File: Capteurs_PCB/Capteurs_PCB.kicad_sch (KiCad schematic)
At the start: 24 parts, among them J1 Conn_01x04, J101 Conn_01x03, J103 Conn_02x20_Odd_Even, J104 Conn_ST_STDC14, J2 Conn_01x03, J3 Alim_Prop2, J4 Conn_01x02, J5 Alim_Prop1, J6 Conn_01x03, J7 Conn_01x03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

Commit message: Problème réglé
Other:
- sheet Regulation ports: added 12V; removed 7.4V
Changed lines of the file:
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@@
-    )
-  )
-  (symbol (lib_id "power:+7.5V") (at 143.51 114.3 270) (unit 1)
-    (in_bom yes) (on_board yes) (dnp no) (fields_autoplaced)
-    (property "Reference" "#PWR0119" (at 139.7 114.3 0)
-      (effects (font (size 1.27 1.27)) hide)
-    )
-    (property "Value" "+7.4V" (at 147.32 114.935 90)
-      (effects (font (size 1.27 1.27)) (justify left))
-    )
-    (property "Footprint" "" (at 143.51 114.3 0)
-      (effects (font (size 1.27 1.27)) hide)
-    )
-    (property "Datasheet" "" (at 143.51 114.3 0)
-      (effects (font (size 1.27 1.27)) hide)
-    )
-    (pin "1")
-    (instances
-      (project "Capteurs_PCB"
-        (path "/1101af8f-9425-4102-9245-339dc54562bf"
-          (reference "#PWR0119") (unit 1)
-        )
-      )
     )
   )
@@
       (effects (font (size 1.27 1.27)) (justify right))
     )
-    (pin "7.4V" input (at 142.24 114.3 0)
+    (pin "12V" input (at 142.24 114.3 0)
       (effects (font (size 1.27 1.27)) (justify right))
     )

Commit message: modifs kicad
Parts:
- removed J3: Alim_Prop2, Connector_Hirose:Hirose_DF13-02P-1.25DSA_1x02_P1.25mm_Vertical, symbol Connector:Conn_01x02_Socket
- removed J5: Alim_Prop1, Connector_Hirose:Hirose_DF13-02P-1.25DSA_1x02_P1.25mm_Vertical, symbol Connector:Conn_01x02_Socket
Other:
- sheet Regulation ports: added 7.5V; removed 12V
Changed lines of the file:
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@@
+    (stroke (width 0) (type default))
+  )
+  (wire (pts (xy 62.23 76.2) (xy 68.58 76.2))
     (stroke (width 0) (type default))
   )
@@
     (stroke (width 0) (type default))
   )
-  (wire (pts (xy 212.09 45.72) (xy 224.79 45.72))
-    (stroke (width 0) (type default))
-  )
   (wire (pts (xy 105.41 114.3) (xy 114.3 114.3))
     (stroke (width 0) (type default))
@@
     (stroke (width 0) (type default))
   )
-  (wire (pts (xy 176.53 46.99) (xy 187.96 46.99))
-    (stroke (width 0) (type default))
-  )
   (wire (pts (xy 144.78 39.37) (xy 143.51 39.37))
     (stroke (width 0) (type default))
@@
     (stroke (width 0) (type default))
   )
-  (wire (pts (xy 176.53 49.53) (xy 176.53 50.8))
-    (stroke (width 0) (type default))
-  )
   (wire (pts (xy 224.79 77.47) (xy 226.06 77.47))
     (stroke (width 0) (type default))
@@
     (stroke (width 0) (type default))
   )
-  (wire (pts (xy 212.09 48.26) (xy 213.36 48.26))
-    (stroke (width 0) (type default))
-  )
   (wire (pts (xy 144.78 62.23) (xy 144.78 54.61))
     (stroke (width 0) (type default))
@@
   )
   (wire (pts (xy 46.99 66.04) (xy 46.99 62.23))
-    (stroke (width 0) (type default))
-  )
-  (wire (pts (xy 213.36 48.26) (xy 213.36 49.53))
     (stroke (width 0) (type default))
   )
@@
     (effects (font (size 1.27 1.27)) (justify right bottom))
   )
-  (label "V_ALIM_PROP1" (at 187.96 46.99 180) (fields_autoplaced)
-    (effects (font (size 1.27 1.27)) (justify right bottom))
-  )
   (label "Sig_LED" (at 102.87 91.44 180) (fields_autoplaced)
     (effects (font (size 1.27 1.27)) (justify right bottom))
@@
     (effects (font (size 1.27 1.27)) (justify right bottom))
   )
-  (label "V_ALIM_PROP2" (at 224.79 45.72 180) (fields_autoplaced)
+  (label "DATA1" (at 68.58 76.2 180) (fields_autoplaced)
     (effects (font (size 1.27 1.27)) (justify right bottom))
   )
@@
     (effects (font (size 1.27 1.27)) (justify left))
     (property "Intersheetrefs" "${INTERSHEET_REFS}" (at 235.9205 74.93 0)
-      (effects (font (size 1.27 1.27)) (justify left) hide)
-    )
-  )
-  (global_label "DATA1" (shape input) (at 62.23 76.2 0) (fields_autoplaced)
-    (effects (font (size 1.27 1.27)) (justify left))
-    (property "Intersheetrefs" "${INTERSHEET_REFS}" (at 70.7601 76.2 0)
       (effects (font (size 1.27 1.27)) (justify left) hide)
     )
@@
         (path "/1101af8f-9425-4102-9245-339dc54562bf"
           (reference "#PWR040") (unit 1)
-        )
-      )
-    )
-  )
-  (symbol (lib_id "Connector:Conn_01x02_Socket") (at 207.01 48.26 180) (unit 1)
-    (in_bom yes) (on_board yes) (dnp no)
-    (property "Reference" "J3" (at 207.01 39.37 0)
-      (effects (font (size 1.27 1.27)))
-    )
-    (property "Value" "Alim_Prop2" (at 207.01 41.91 0)
-      (effects (font (size 1.27 1.27)))
-    )
-    (property "Footprint" "Connector_Hirose:Hirose_DF13-02P-1.25DSA_1x02_P1.25mm_Vertical" (at 207.01 48.26 0)
-      (effects (font (size 1.27 1.27)) hide)
-    )
-    (property "Datasheet" "~" (at 207.01 48.26 0)
-      (effects (font (size 1.27 1.27)) hide)
-    )
-    (pin "1")
-    (pin "2")
-    (instances
-      (project "Capteurs_PCB"
-        (path "/1101af8f-9425-4102-9245-339dc54562bf"
-          (reference "J3") (unit 1)
         )
       )
@@
     )
   )
-  (symbol (lib_id "power:GND") (at 176.53 50.8 0) (unit 1)
-    (in_bom yes) (on_board yes) (dnp no)
-    (property "Reference" "#PWR010" (at 176.53 57.15 0)
-      (effects (font (size 1.27 1.27)) hide)
-    )
-    (property "Value" "GND" (at 176.53 55.88 0)
-      (effects (font (size 1.27 1.27)))
-    )
-    (property "Footprint" "" (at 176.53 50.8 0)
-      (effects (font (size 1.27 1.27)) hide)
-    )
-    (property "Datasheet" "" (at 176.53 50.8 0)
-      (effects (font (size 1.27 1.27)) hide)
-    )
-    (pin "1")
-    (instances
-      (project "Capteurs_PCB"
-        (path "/1101af8f-9425-4102-9245-339dc54562bf"
-          (reference "#PWR010") (unit 1)
-        )
-      )
-    )
-  )
   (symbol (lib_id "Connector_Generic:Conn_01x02") (at 238.76 30.48 180) (unit 1)
     (in_bom yes) (on_board yes) (dnp no) (fields_autoplaced)
@@
     )
   )
-  (symbol (lib_id "power:GND") (at 213.36 49.53 0) (unit 1)
-    (in_bom yes) (on_board yes) (dnp no)
-    (property "Reference" "#PWR011" (at 213.36 55.88 0)
-      (effects (font (size 1.27 1.27)) hide)
-    )
-    (property "Value" "GND" (at 213.36 54.61 0)
-      (effects (font (size 1.27 1.27)))
-    )
-    (property "Footprint" "" (at 213.36 49.53 0)
-      (effects (font (size 1.27 1.27)) hide)
-    )
-    (property "Datasheet" "" (at 213.36 49.53 0)
-      (effects (font (size 1.27 1.27)) hide)
-    )
-    (pin "1")
-    (instances
-      (project "Capteurs_PCB"
-        (path "/1101af8f-9425-4102-9245-339dc54562bf"
-          (reference "#PWR011") (unit 1)
-        )
-      )
-    )
-  )
   (symbol (lib_id "power:+BATT") (at 88.9 114.3 0) (unit 1)
     (in_bom yes) (on_board yes) (dnp no)
@@
         (path "/1101af8f-9425-4102-9245-339dc54562bf"
           (reference "#PWR0120") (unit 1)
+        )
+      )
+    )
+  )
+  (symbol (lib_id "power:+7.5V") (at 143.51 114.3 270) (unit 1)
+    (in_bom yes) (on_board yes) (dnp no) (fields_autoplaced)
+    (property "Reference" "#PWR010" (at 139.7 114.3 0)
+      (effects (font (size 1.27 1.27)) hide)
+    )
+    (property "Value" "+7.5V" (at 147.32 114.935 90)
+      (effects (font (size 1.27 1.27)) (justify left))
+    )
+    (property "Footprint" "" (at 143.51 114.3 0)
+      (effects (font (size 1.27 1.27)) hide)
+    )
+    (property "Datasheet" "" (at 143.51 114.3 0)
+      (effects (font (size 1.27 1.27)) hide)
+    )
+    (pin "1")
+    (instances
+      (project "Capteurs_PCB"
+        (path "/1101af8f-9425-4102-9245-339dc54562bf"
+          (reference "#PWR010") (unit 1)
         )
       )
@@
     )
   )
-  (symbol (lib_id "Connector:Conn_01x02_Socket") (at 171.45 49.53 180) (unit 1)
-    (in_bom yes) (on_board yes) (dnp no)
-    (property "Reference" "J5" (at 171.45 40.64 0)
-      (effects (font (size 1.27 1.27)))
-    )
-    (property "Value" "Alim_Prop1" (at 171.45 43.18 0)
-      (effects (font (size 1.27 1.27)))
-    )
-    (property "Footprint" "Connector_Hirose:Hirose_DF13-02P-1.25DSA_1x02_P1.25mm_Vertical" (at 171.45 49.53 0)
-      (effects (font (size 1.27 1.27)) hide)
-    )
-    (property "Datasheet" "~" (at 171.45 49.53 0)
-      (effects (font (size 1.27 1.27)) hide)
-    )
-    (pin "1")
-    (pin "2")
-    (instances
-      (project "Capteurs_PCB"
-        (path "/1101af8f-9425-4102-9245-339dc54562bf"
-          (reference "J5") (unit 1)
-        )
-      )
-    )
-  )
   (symbol (lib_id "power:PWR_FLAG") (at 91.44 116.84 180) (unit 1)
     (in_bom yes) (on_board yes) (dnp no) (fields_autoplaced)
@@
       (effects (font (size 1.27 1.27)) (justify right))
     )
-    (pin "12V" input (at 142.24 114.3 0)
+    (pin "7.5V" input (at 142.24 114.3 0)
       (effects (font (size 1.27 1.27)) (justify right))
     )

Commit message: Changement Label
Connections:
- net ST-RX renamed ST_RX

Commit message: Suite PCB
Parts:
- removed SW101: SW_DPDT_x2, Button_Switch_SMD:SW_DPDT_CK_JS202011JCQN, symbol Switch:SW_DPDT_x2
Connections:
- no-connect marks 40 -> 39
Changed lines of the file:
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@@
   (junction (at 144.78 62.23) (diameter 0) (color 0 0 0 0)
-  )
-  (junction (at 91.44 116.84) (diameter 0) (color 0 0 0 0)
   )
   (junction (at 49.53 62.23) (diameter 0) (color 0 0 0 0)
@@
   (no_connect (at 97.79 64.77))
   (no_connect (at 110.49 54.61))
-  (no_connect (at 95.25 121.92))
   (no_connect (at 110.49 69.85))
   (no_connect (at 97.79 44.45))
@@
     (stroke (width 0) (type default))
   )
-  (wire (pts (xy 62.23 76.2) (xy 67.564 76.2))
+  (wire (pts (xy 62.23 76.2) (xy 67.31 76.2))
     (stroke (width 0) (type default))
   )
@@
     (stroke (width 0) (type default))
   )
-  (wire (pts (xy 105.41 114.3) (xy 114.3 114.3))
+  (wire (pts (xy 109.22 114.3) (xy 114.3 114.3))
     (stroke (width 0) (type default))
   )
@@
     (stroke (width 0) (type default))
   )
-  (wire (pts (xy 202.692 116.84) (xy 195.58 116.84))
+  (wire (pts (xy 201.93 116.84) (xy 195.58 116.84))
     (stroke (width 0) (type default))
   )
@@
     (stroke (width 0) (type default))
   )
-  (wire (pts (xy 105.41 119.38) (xy 105.41 114.3))
-    (stroke (width 0) (type default))
-  )
   (wire (pts (xy 62.23 73.66) (xy 67.31 73.66))
     (stroke (width 0) (type default))
@@
     (stroke (width 0) (type default))
   )
-  (wire (pts (xy 88.9 116.84) (xy 91.44 116.84))
-    (stroke (width 0) (type default))
-  )
   (wire (pts (xy 49.53 59.69) (xy 49.53 62.23))
     (stroke (width 0) (type default))
@@
     (stroke (width 0) (type default))
   )
-  (wire (pts (xy 202.946 119.38) (xy 195.58 119.38))
+  (wire (pts (xy 201.93 119.38) (xy 195.58 119.38))
     (stroke (width 0) (type default))
   )
@@
     (stroke (width 0) (type default))
   )
-  (wire (pts (xy 88.9 114.3) (xy 88.9 116.84))
-    (stroke (width 0) (type default))
-  )
   (wire (pts (xy 243.84 30.48) (xy 246.38 30.48))
     (stroke (width 0) (type default))
@@
     (stroke (width 0) (type default))
   )
-  (wire (pts (xy 91.44 116.84) (xy 95.25 116.84))
-    (stroke (width 0) (type default))
-  )
   (wire (pts (xy 30.48 67.31) (xy 30.48 71.12))
     (stroke (width 0) (type default))
@@
     (stroke (width 0) (type default))
   )
-  (wire (pts (xy 28.956 91.44) (xy 36.83 91.44))
+  (wire (pts (xy 29.21 91.44) (xy 36.83 91.44))
     (stroke (width 0) (type default))
   )
@@
     (effects (font (size 1.27 1.27)) (justify right bottom))
   )
-  (label "ST_TX" (at 202.946 119.38 180) (fields_autoplaced)
+  (label "ST_TX" (at 201.93 119.38 180) (fields_autoplaced)
     (effects (font (size 1.27 1.27)) (justify right bottom))
   )
@@
     (effects (font (size 1.27 1.27)) (justify right bottom))
   )
-  (label "ST_RX" (at 202.692 116.84 180) (fields_autoplaced)
+  (label "ST_RX" (at 201.93 116.84 180) (fields_autoplaced)
     (effects (font (size 1.27 1.27)) (justify right bottom))
   )
@@
     (effects (font (size 1.27 1.27)) (justify left bottom))
   )
-  (label "ST_RX" (at 28.956 91.44 0) (fields_autoplaced)
+  (label "ST_RX" (at 29.21 91.44 0) (fields_autoplaced)
     (effects (font (size 1.27 1.27)) (justify left bottom))
   )
@@
     (effects (font (size 1.27 1.27)) (justify left bottom))
   )
-  (label "DATA1" (at 67.564 76.2 180) (fields_autoplaced)
+  (label "DATA1" (at 67.31 76.2 180) (fields_autoplaced)
     (effects (font (size 1.27 1.27)) (justify right bottom))
   )
@@
     )
   )
-  (symbol (lib_id "Switch:SW_DPDT_x2") (at 100.33 119.38 180) (unit 1)
-    (in_bom yes) (on_board yes) (dnp no)
-    (property "Reference" "SW101" (at 99.06 127 0)
-      (effects (font (size 1.27 1.27)))
-    )
-    (property "Value" "SW_DPDT_x2" (at 97.79 124.46 0)
-      (effects (font (size 1.27 1.27)))
-    )
-    (property "Footprint" "Button_Switch_SMD:SW_DPDT_CK_JS202011JCQN" (at 100.33 119.38 0)
-      (effects (font (size 1.27 1.27)) hide)
-    )
-    (property "Datasheet" "~" (at 100.33 119.38 0)
-      (effects (font (size 1.27 1.27)) hide)
-    )
-    (pin "1")
-    (pin "2")
-    (pin "3")
-    (pin "4")
-    (pin "5")
-    (pin "6")
-    (instances
-      (project "Capteurs_PCB"
-        (path "/1101af8f-9425-4102-9245-339dc54562bf"
-          (reference "SW101") (unit 1)
-        )
-      )
-    )
-  )
   (symbol (lib_id "power:GND") (at 213.36 34.29 0) (unit 1)
     (in_bom yes) (on_board yes) (dnp no) (fields_autoplaced)
@@
     )
   )
-  (symbol (lib_id "power:+BATT") (at 88.9 114.3 0) (unit 1)
+  (symbol (lib_id "power:+BATT") (at 109.22 114.3 0) (unit 1)
     (in_bom yes) (on_board yes) (dnp no)
-    (property "Reference" "#PWR0120" (at 88.9 118.11 0)
-      (effects (font (size 1.27 1.27)) hide)
-    )
-    (property "Value" "+BATT" (at 84.074 113.538 0)
-      (effects (font (size 1.27 1.27)))
-    )
-    (property "Footprint" "" (at 88.9 114.3 0)
-      (effects (font (size 1.27 1.27)) hide)
-    )
-    (property "Datasheet" "" (at 88.9 114.3 0)
+    (property "Reference" "#PWR0120" (at 109.22 118.11 0)
+      (effects (font (size 1.27 1.27)) hide)
+    )
+    (property "Value" "+BATT" (at 104.394 113.538 0)
+      (effects (font (size 1.27 1.27)))
+    )
+    (property "Footprint" "" (at 109.22 114.3 0)
+      (effects (font (size 1.27 1.27)) hide)
+    )
+    (property "Datasheet" "" (at 109.22 114.3 0)
       (effects (font (size 1.27 1.27)) hide)
     )
@@
         )
       )
-    )
-  )
-  (symbol (lib_id "power:PWR_FLAG") (at 91.44 116.84 180) (unit 1)
-    (in_bom yes) (on_board yes) (dnp no) (fields_autoplaced)
-    (property "Reference" "#FLG01" (at 91.44 118.745 0)
-      (effects (font (size 1.27 1.27)) hide)
-    )
-    (property "Value" "PWR_FLAG" (at 91.44 121.92 0)
-      (effects (font (size 1.27 1.27)))
-    )
-    (property "Footprint" "" (at 91.44 116.84 0)
-      (effects (font (size 1.27 1.27)) hide)
-    )
-    (property "Datasheet" "~" (at 91.44 116.84 0)
-      (effects (font (size 1.27 1.27)) hide)
-    )
-    (pin "1")
-    (instances
-      (project "Capteurs_PCB"
-        (path "/1101af8f-9425-4102-9245-339dc54562bf"
-          (reference "#FLG01") (unit 1)
-        )
-      )

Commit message: Début de routage
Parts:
- J1: footprint Connector_PinSocket_2.54mm:PinSocket_1x04_P2.54mm_Vertical -> Connector_JST:JST_XH_B4B-XH-A_1x04_P2.50mm_Vertical
- J101, J6, J7: footprint Connector_PinHeader_2.54mm:PinHeader_1x03_P2.54mm_Vertical -> Connector_JST:JST_XH_B3B-XH-A_1x03_P2.50mm_Vertical
- J2: footprint Connector_PinSocket_2.54mm:PinSocket_1x03_P2.54mm_Vertical -> Connector_JST:JST_XH_B3B-XH-A_1x03_P2.50mm_Vertical
- J4: footprint Connector_PinHeader_2.54mm:PinHeader_1x02_P2.54mm_Vertical -> Connector_AMASS:AMASS_XT60-M_1x02_P7.20mm_Vertical
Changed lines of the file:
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@@
       (effects (font (size 1.27 1.27)))
     )
-    (property "Footprint" "Connector_PinHeader_2.54mm:PinHeader_1x03_P2.54mm_Vertical" (at 219.71 74.93 0)
+    (property "Footprint" "Connector_JST:JST_XH_B3B-XH-A_1x03_P2.50mm_Vertical" (at 219.71 74.93 0)
       (effects (font (size 1.27 1.27)) hide)
     )
@@
       (effects (font (size 1.27 1.27)))
     )
-    (property "Footprint" "Connector_PinSocket_2.54mm:PinSocket_1x03_P2.54mm_Vertical" (at 207.01 30.48 0)
+    (property "Footprint" "Connector_JST:JST_XH_B3B-XH-A_1x03_P2.50mm_Vertical" (at 207.01 30.48 0)
       (effects (font (size 1.27 1.27)) hide)
     )
@@
       (effects (font (size 1.27 1.27)))
     )
-    (property "Footprint" "Connector_PinHeader_2.54mm:PinHeader_1x03_P2.54mm_Vertical" (at 241.3 74.93 0)
+    (property "Footprint" "Connector_JST:JST_XH_B3B-XH-A_1x03_P2.50mm_Vertical" (at 241.3 74.93 0)
       (effects (font (size 1.27 1.27)) hide)
     )
@@
       (effects (font (size 1.27 1.27)))
     )
-    (property "Footprint" "Connector_PinHeader_2.54mm:PinHeader_1x02_P2.54mm_Vertical" (at 238.76 30.48 0)
+    (property "Footprint" "Connector_AMASS:AMASS_XT60-M_1x02_P7.20mm_Vertical" (at 238.76 30.48 0)
       (effects (font (size 1.27 1.27)) hide)
     )
@@
       (effects (font (size 1.27 1.27)))
     )
-    (property "Footprint" "Connector_PinHeader_2.54mm:PinHeader_1x03_P2.54mm_Vertical" (at 170.18 30.48 0)
+    (property "Footprint" "Connector_JST:JST_XH_B3B-XH-A_1x03_P2.50mm_Vertical" (at 170.18 30.48 0)
       (effects (font (size 1.27 1.27)) hide)
     )
@@
       (effects (font (size 1.27 1.27)))
     )
-    (property "Footprint" "Connector_PinSocket_2.54mm:PinSocket_1x04_P2.54mm_Vertical" (at 88.9 96.52 0)
-      (effects (font (size 1.27 1.27)) hide)
-    )
+    (property "Footprint" "Connector_JST:JST_XH_B4B-XH-A_1x04_P2.50mm_Vertical" (at 88.9 96.52 0)
+      (effects (font (size 1.27 1.27)) hide)
+    )

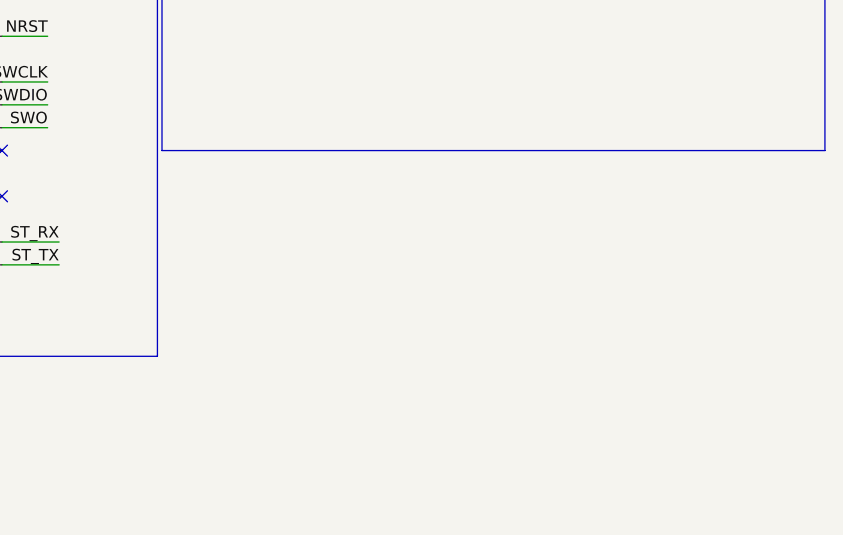
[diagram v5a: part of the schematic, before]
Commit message: Add POE Injector
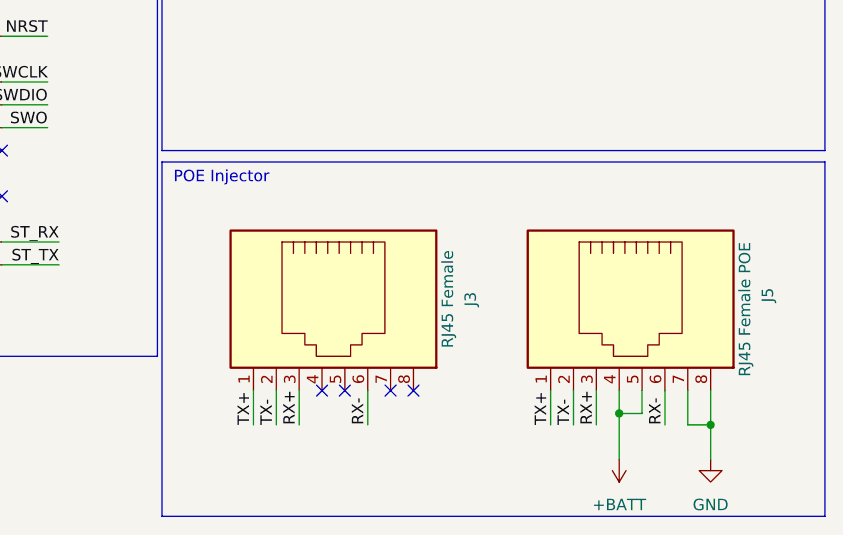
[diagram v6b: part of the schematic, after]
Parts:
- added J3: RJ45 Female, symbol Connector:RJ45
- added J5: RJ45 Female POE, symbol Connector:RJ45
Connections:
- net +BATT: now also J5.4, J5.5
- net GND: now also J5.7, J5.8
- new net RX+: J3.3, J5.3
- new net RX-: J3.6, J5.6
- new net TX+: J3.1, J5.1
- new net TX-: J3.2, J5.2
- no-connect marks 39 -> 43
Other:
- note added: "POE Injector"

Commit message: Routage
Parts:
- removed J3: RJ45 Female, symbol Connector:RJ45
- removed J5: RJ45 Female POE, symbol Connector:RJ45
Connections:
- no-connect marks 43 -> 39
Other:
- note removed: "POE Injector"
